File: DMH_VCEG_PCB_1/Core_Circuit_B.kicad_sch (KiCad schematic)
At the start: 111 parts, among them J24 Conn_01x06_PinHeader, J25 Conn_01x10_PinHeader, J26 Conn_01x10_PinHeader, J27 Conn_01x10_PinHeader, Q17 BC558, Q18 BC558, Q19 BC548, Q20 BC548, Q21 BS170, Q22 BS170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

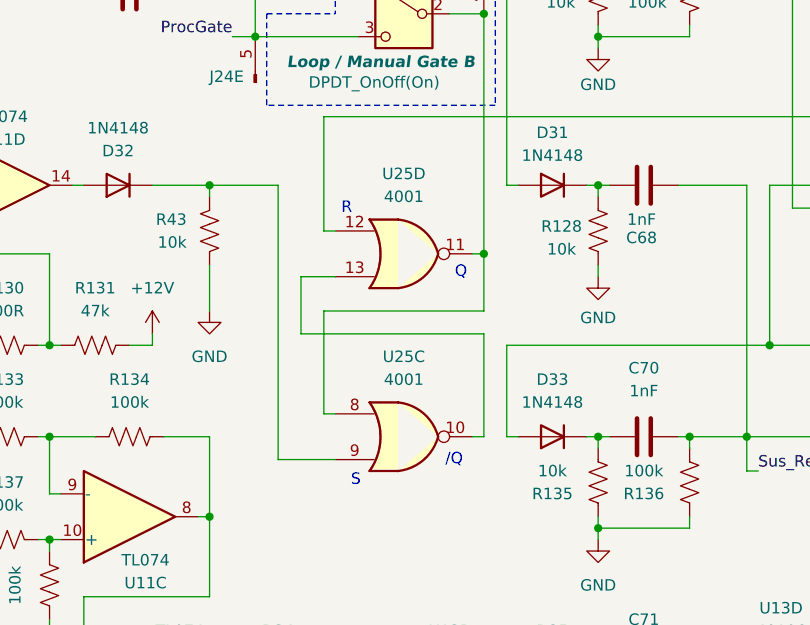
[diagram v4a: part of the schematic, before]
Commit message: PCB 1 placement in progress
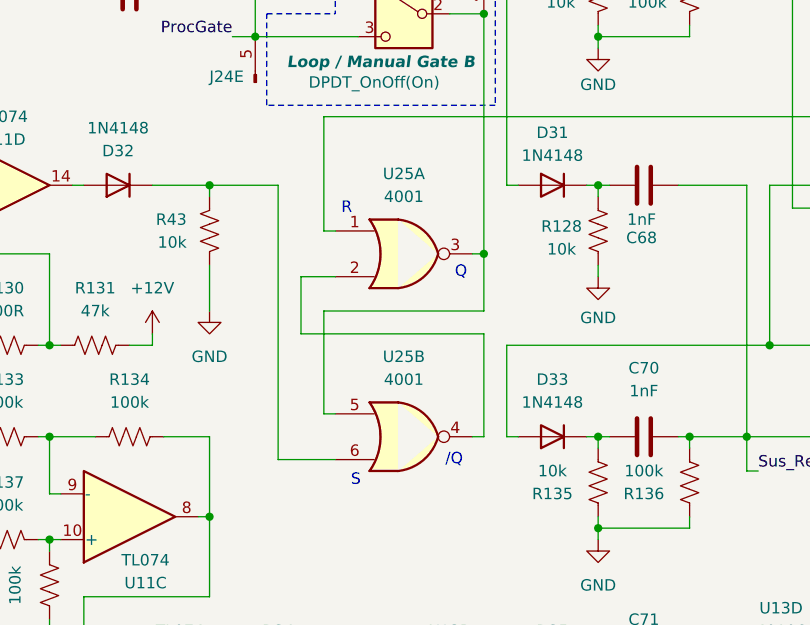
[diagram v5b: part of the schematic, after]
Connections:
- net at D32.1 (K), R43.2: now also U25.6; no longer U25.9
- net at C56.1, R129.1: now also U25.1; no longer U25.12
- net at J24.4 (Pin_4), SW5.2 (B): now also U25.3, U25.5; no longer U25.11, U25.8
- new net: U25.2, U25.4
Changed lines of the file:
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@@
 		(lib_id "4xxx:4001")
 		(at 76.2 151.13 0)
-		(unit 3)
+		(unit 2)
 		(exclude_from_sim no)
 		(in_bom yes)
@@
 				(path "/58f4306d-5387-4983-bb08-41a2313fd315/8d22a13f-1d3b-4a1f-8b3f-baf42965c019"
 					(reference "U25")
-					(unit 3)
+					(unit 2)
 				)
 			)
@@
 		(lib_id "4xxx:4001")
 		(at 76.2 130.81 0)
-		(unit 4)
+		(unit 1)
 		(exclude_from_sim no)
 		(in_bom yes)
@@
 				(path "/58f4306d-5387-4983-bb08-41a2313fd315/8d22a13f-1d3b-4a1f-8b3f-baf42965c019"
 					(reference "U25")
-					(unit 4)
-				)
-			)
+					(unit 1)
+				)
+			)

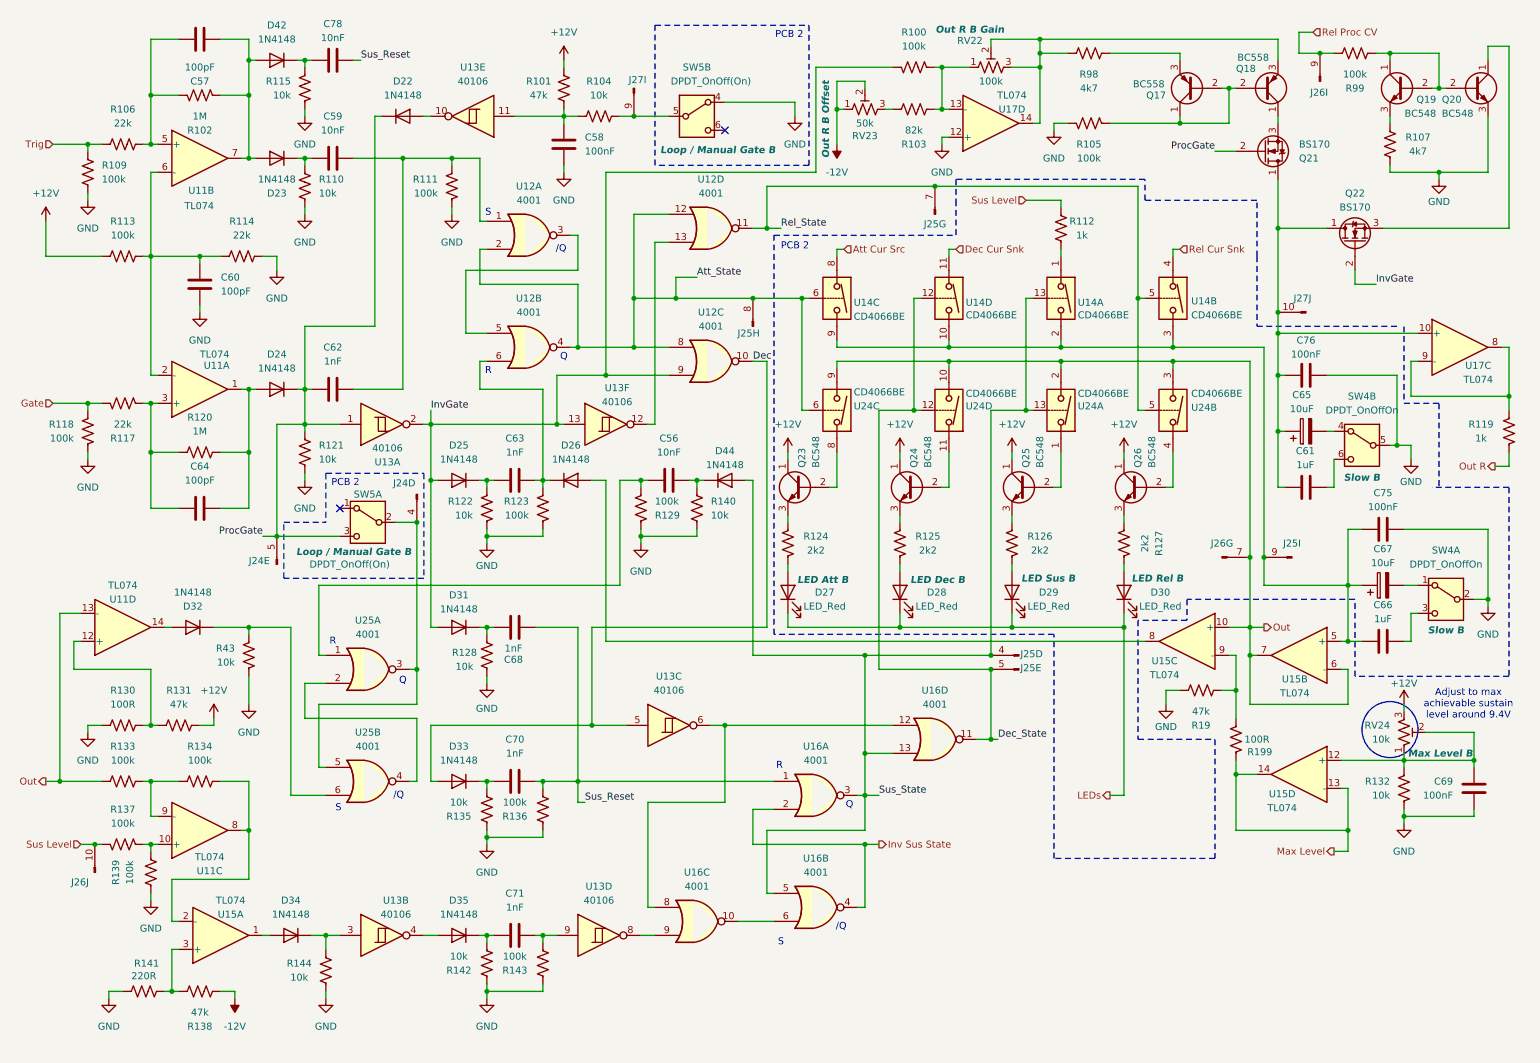
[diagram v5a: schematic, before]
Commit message: PCB 1 circuit A placement done
ciurcuit B placement in progress
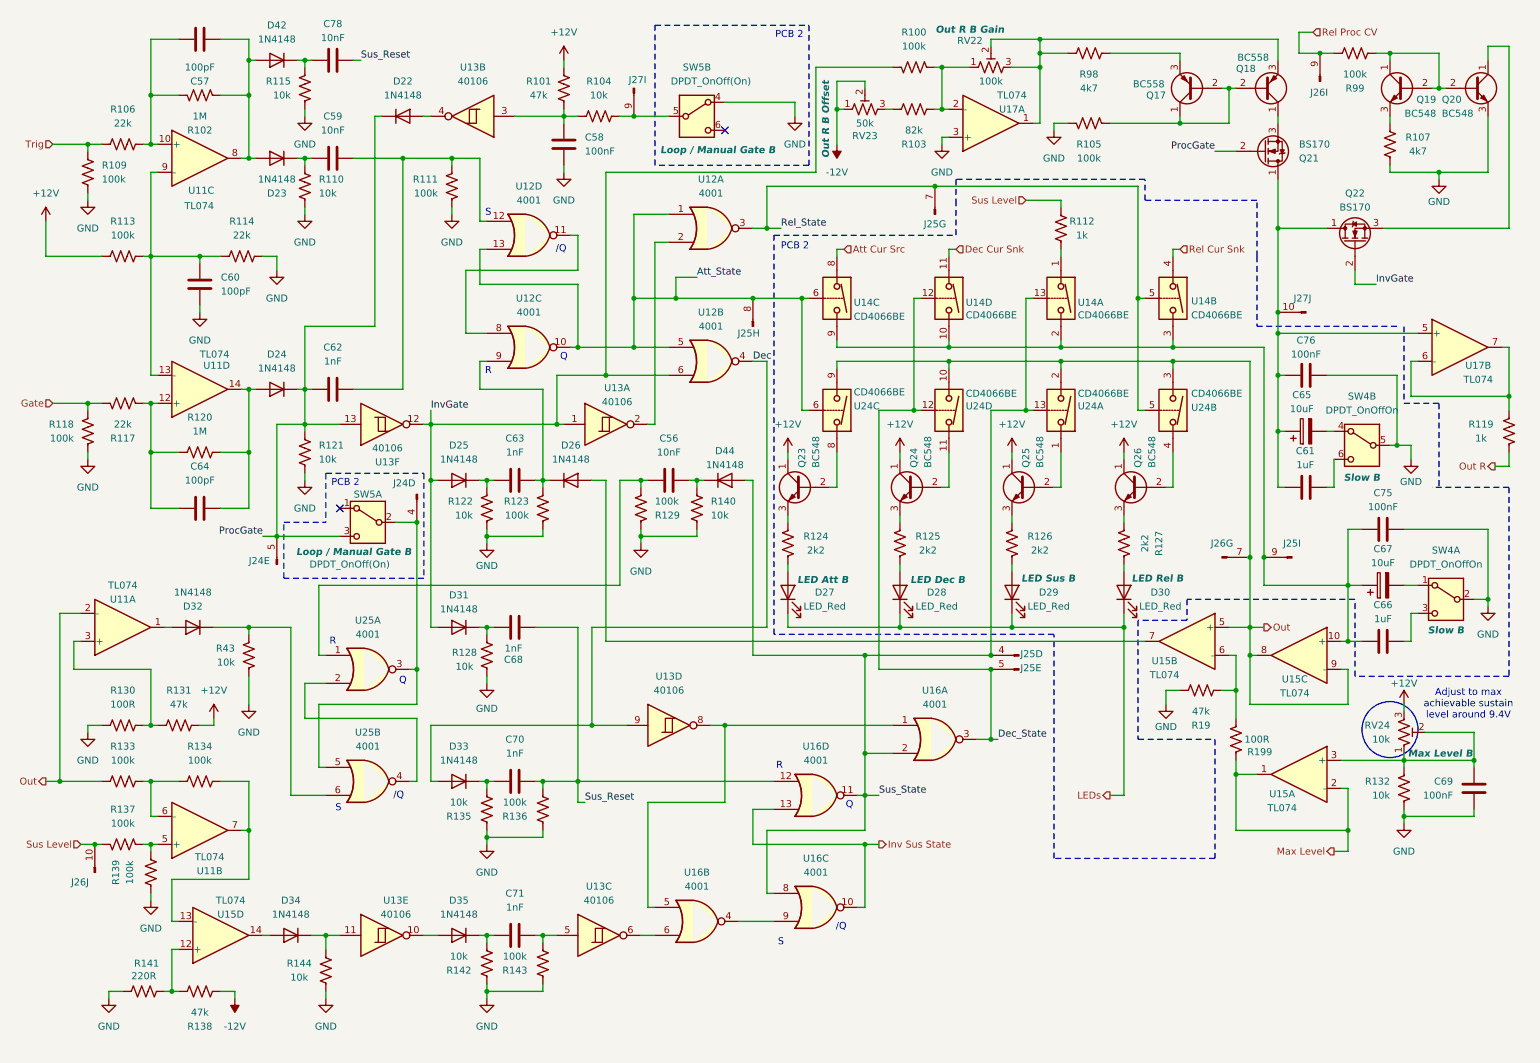
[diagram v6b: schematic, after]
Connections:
- net Att_State: now also U12.1, U12.10, U12.13, U12.5; no longer U12.12, U12.2, U12.4, U12.8
- net Dec: now also U12.4, U13.9; no longer U12.10, U13.5
- net Dec_State: now also U16.3; no longer U16.11
- net GND: now also U17.3 (+); no longer U17.12 (+)
- net Inv Sus State: now also U16.10, U16.13; no longer U16.2, U16.4
- net InvGate: now also U12.6, U13.1, U13.12; no longer U12.9, U13.13, U13.2
- net Max Level: now also U15.1, U15.2 (-); no longer U15.13 (-), U15.14
- net Out: now also U11.2 (-), U15.5 (+), U15.8, U15.9 (-); no longer U11.13 (-), U15.10 (+), U15.6 (-), U15.7
- net ProcGate: now also U13.13; no longer U13.1
- net Rel_State: now also U12.3; no longer U12.11
- net Sus_Reset: now also U16.12; no longer U16.1
- net Sus_State: now also U16.11, U16.2, U16.8; no longer U16.13, U16.3, U16.5
- net at C61.2, C65.1, C76.2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: now also U17.5 (+); no longer U17.10 (+)
- net at D32.2 (A): now also U11.1; no longer U11.14
- net at C60.2, R113.1, R114.2: now also U11.13 (-), U11.9 (-); no longer U11.2 (-), U11.6 (-)
- net at C59.2, C62.2, R111.2: now also U12.12; no longer U12.1
- net at C57.2, D23.2 (A), D42.2 (A)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: now also U11.8; no longer U11.7
- net at R137.2, R139.1: now also U11.5 (+); no longer U11.10 (+)
- net at R133.1, R134.2: now also U11.6 (-); no longer U11.9 (-)
- net at D22.2 (A): now also U13.4; no longer U13.10
- net at R19.2, R199.1: now also U15.6 (-); no longer U15.9 (-)
- net at C63.2, D26.1 (K), R123.2: now also U12.9; no longer U12.6
- net at C64.2, D24.2 (A), R120.1: now also U11.14; no longer U11.1
- net at C64.1, R117.1, R120.2: now also U11.12 (+); no longer U11.3 (+)
- net at D26.2 (A): now also U15.7; no longer U15.8
- net at C58.1, R101.2, R104.2: now also U13.3; no longer U13.11
- net at C69.2, R132.2, RV24.1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: now also U15.3 (+); no longer U15.12 (+)
- net at C66.1, C67.1, C75.2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: now also U15.10 (+); no longer U15.5 (+)
- net at C57.1, R102.2, R106.1: now also U11.10 (+); no longer U11.5 (+)
- net at R100.2, R103.2, RV22.1: now also U17.2 (-); no longer U17.13 (-)
- net at Q18.3 (E), R98.1, RV22.2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: now also U17.1; no longer U17.14
- net at D34.2 (A): now also U15.14; no longer U15.1
- net at R138.1, R141.1: now also U15.12 (+); no longer U15.3 (+)
- net at R130.1, R131.2: now also U11.3 (+); no longer U11.12 (+)
- net at D34.1 (K), R144.1: now also U13.11; no longer U13.3
- net at D35.2 (A): now also U13.10; no longer U13.4
- net at C71.2, R143.1: now also U13.5; no longer U13.9
- new net: R134.1, U11.7, U15.13 (-)
- new net: U12.11, U12.8
- new net: U12.2, U13.2
- new net: U13.8, U16.1, U16.5
- new net: U16.4, U16.9
- new net: U13.6, U16.6
- new net: R119.2, U17.6 (-), U17.7
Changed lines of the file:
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@@
 		(at 45.72 160.02 0)
 		(mirror x)
-		(unit 3)
+		(unit 2)
 		(exclude_from_sim no)
 		(in_bom yes)
@@
 				(path "/58f4306d-5387-4983-bb08-41a2313fd315/8d22a13f-1d3b-4a1f-8b3f-baf42965c019"
 					(reference "U11")
-					(unit 3)
+					(unit 2)
 				)
 			)
@@
 		(lib_id "4xxx:4001")
 		(at 105.41 72.39 0)
-		(unit 2)
+		(unit 3)
 		(exclude_from_sim no)
 		(in_bom yes)
@@
 				(path "/58f4306d-5387-4983-bb08-41a2313fd315/8d22a13f-1d3b-4a1f-8b3f-baf42965c019"
 					(reference "U12")
-					(unit 2)
+					(unit 3)
 				)
 			)
@@
 		(lib_id "4xxx:4001")
 		(at 138.43 74.93 0)
-		(unit 3)
+		(unit 2)
 		(exclude_from_sim no)
 		(in_bom yes)
@@
 				(path "/58f4306d-5387-4983-bb08-41a2313fd315/8d22a13f-1d3b-4a1f-8b3f-baf42965c019"
 					(reference "U12")
-					(unit 3)
+					(unit 2)
 				)
 			)
@@
 		(at 224.79 125.73 0)
 		(mirror y)
-		(unit 3)
+		(unit 2)
 		(exclude_from_sim no)
 		(in_bom yes)
@@
 				(path "/58f4306d-5387-4983-bb08-41a2313fd315/8d22a13f-1d3b-4a1f-8b3f-baf42965c019"
 					(reference "U15")
-					(unit 3)
+					(unit 2)
 				)
 			)
@@
 		(lib_id "4xxx:40106")
 		(at 119.38 86.36 0)
-		(unit 6)
+		(unit 1)
 		(exclude_from_sim no)
 		(in_bom yes)
@@
 				(path "/58f4306d-5387-4983-bb08-41a2313fd315/8d22a13f-1d3b-4a1f-8b3f-baf42965c019"
 					(reference "U13")
-					(unit 6)
+					(unit 1)
 				)
 			)
@@
 		(lib_id "4xxx:40106")
 		(at 95.25 30.48 180)
-		(unit 5)
+		(unit 2)
 		(exclude_from_sim no)
 		(in_bom yes)
@@
 				(path "/58f4306d-5387-4983-bb08-41a2313fd315/8d22a13f-1d3b-4a1f-8b3f-baf42965c019"
 					(reference "U13")
-					(unit 5)
+					(unit 2)
 				)
 			)
@@
 		(lib_id "4xxx:4001")
 		(at 105.41 52.07 0)
-		(unit 1)
+		(unit 4)
 		(exclude_from_sim no)
 		(in_bom yes)
@@
 				(path "/58f4306d-5387-4983-bb08-41a2313fd315/8d22a13f-1d3b-4a1f-8b3f-baf42965c019"
 					(reference "U12")
-					(unit 1)
+					(unit 4)
 				)
 			)
@@
 		(at 245.11 149.86 0)
 		(mirror y)
-		(unit 4)
+		(unit 1)
 		(exclude_from_sim no)
 		(in_bom yes)
@@
 				(path "/58f4306d-5387-4983-bb08-41a2313fd315/8d22a13f-1d3b-4a1f-8b3f-baf42965c019"
 					(reference "U15")
-					(unit 4)
+					(unit 1)
 				)
 			)
@@
 		(at 245.11 128.27 0)
 		(mirror y)
-		(unit 2)
+		(unit 3)
 		(exclude_from_sim no)
 		(in_bom yes)
@@
 				(path "/58f4306d-5387-4983-bb08-41a2313fd315/8d22a13f-1d3b-4a1f-8b3f-baf42965c019"
 					(reference "U15")
-					(unit 2)
+					(unit 3)
 				)
 			)
@@
 		(at 78.74 86.36 0)
 		(mirror x)
-		(unit 1)
+		(unit 6)
 		(exclude_from_sim no)
 		(in_bom yes)
@@
 				(path "/58f4306d-5387-4983-bb08-41a2313fd315/8d22a13f-1d3b-4a1f-8b3f-baf42965c019"
 					(reference "U13")
-					(unit 1)
+					(unit 6)
 				)
 			)
@@
 		(lib_id "4xxx:40106")
 		(at 130.81 140.97 0)
-		(unit 3)
+		(unit 4)
 		(exclude_from_sim no)
 		(in_bom yes)
@@
 				(path "/58f4306d-5387-4983-bb08-41a2313fd315/8d22a13f-1d3b-4a1f-8b3f-baf42965c019"
 					(reference "U13")
-					(unit 3)
+					(unit 4)
 				)
 			)
@@
 		(at 49.53 179.07 0)
 		(mirror x)
-		(unit 1)
+		(unit 4)
 		(exclude_from_sim no)
 		(in_bom yes)
@@
 				(path "/58f4306d-5387-4983-bb08-41a2313fd315/8d22a13f-1d3b-4a1f-8b3f-baf42965c019"
 					(reference "U15")
-					(unit 1)
+					(unit 4)
 				)
 			)
@@
 		(lib_id "4xxx:4001")
 		(at 157.48 153.67 0)
-		(unit 1)
+		(unit 4)
 		(exclude_from_sim no)
 		(in_bom yes)
@@
 				(path "/58f4306d-5387-4983-bb08-41a2313fd315/8d22a13f-1d3b-4a1f-8b3f-baf42965c019"
 					(reference "U16")
-					(unit 1)
+					(unit 4)
 				)
 			)
@@
 		(lib_id "4xxx:4001")
 		(at 135.89 176.53 0)
-		(unit 3)
+		(unit 2)
 		(exclude_from_sim no)
 		(in_bom yes)
@@
 				(path "/58f4306d-5387-4983-bb08-41a2313fd315/8d22a13f-1d3b-4a1f-8b3f-baf42965c019"
 					(reference "U16")
-					(unit 3)
+					(unit 2)
 				)
 			)
@@
 		(lib_id "Amplifier_Operational:TL074")
 		(at 274.32 72.39 0)
-		(unit 3)
+		(unit 2)
 		(exclude_from_sim no)
 		(in_bom yes)
@@
 				(path "/58f4306d-5387-4983-bb08-41a2313fd315/8d22a13f-1d3b-4a1f-8b3f-baf42965c019"
 					(reference "U17")
-					(unit 3)
+					(unit 2)
 				)
 			)
@@
 		(at 189.23 31.75 0)
 		(mirror x)
-		(unit 4)
+		(unit 1)
 		(exclude_from_sim no)
 		(in_bom yes)
@@
 				(path "/58f4306d-5387-4983-bb08-41a2313fd315/8d22a13f-1d3b-4a1f-8b3f-baf42965c019"
 					(reference "U17")
-					(unit 4)
+					(unit 1)
 				)
 			)
@@
 		(lib_id "4xxx:4001")
 		(at 157.48 173.99 0)
-		(unit 2)
+		(unit 3)
 		(exclude_from_sim no)
 		(in_bom yes)
@@
 				(path "/58f4306d-5387-4983-bb08-41a2313fd315/8d22a13f-1d3b-4a1f-8b3f-baf42965c019"
 					(reference "U16")
-					(unit 2)
+					(unit 3)
 				)
 			)
@@
 		(lib_id "4xxx:40106")
 		(at 78.74 179.07 0)
-		(unit 2)
+		(unit 5)
 		(exclude_from_sim no)
 		(in_bom yes)
@@
 				(path "/58f4306d-5387-4983-bb08-41a2313fd315/8d22a13f-1d3b-4a1f-8b3f-baf42965c019"
 					(reference "U13")
-					(unit 2)
+					(unit 5)
 				)
 			)
@@
 		(lib_id "Amplifier_Operational:TL074")
 		(at 45.72 38.1 0)
-		(unit 2)
+		(unit 3)
 		(exclude_from_sim no)
 		(in_bom yes)
@@
 				(path "/58f4306d-5387-4983-bb08-41a2313fd315/8d22a13f-1d3b-4a1f-8b3f-baf42965c019"
 					(reference "U11")
-					(unit 2)
+					(unit 3)
 				)
 			)
@@
 		(at 31.75 123.19 0)
 		(mirror x)
-		(unit 4)
+		(unit 1)
 		(exclude_from_sim no)
 		(in_bom yes)
@@
 				(path "/58f4306d-5387-4983-bb08-41a2313fd315/8d22a13f-1d3b-4a1f-8b3f-baf42965c019"
 					(reference "U11")
-					(unit 4)
+					(unit 1)
 				)
 			)
@@
 		(at 45.72 80.01 0)
 		(mirror x)
-		(unit 1)
+		(unit 4)
 		(exclude_from_sim no)
 		(in_bom yes)
@@
 				(path "/58f4306d-5387-4983-bb08-41a2313fd315/8d22a13f-1d3b-4a1f-8b3f-baf42965c019"
 					(reference "U11")
-					(unit 1)
+					(unit 4)
 				)
 			)
@@
 		(lib_id "4xxx:4001")
 		(at 138.43 50.8 0)
-		(unit 4)
+		(unit 1)
 		(exclude_from_sim no)
 		(in_bom yes)
@@
 				(path "/58f4306d-5387-4983-bb08-41a2313fd315/8d22a13f-1d3b-4a1f-8b3f-baf42965c019"
 					(reference "U12")
-					(unit 4)
+					(unit 1)
 				)
 			)
@@
 		(lib_id "4xxx:40106")
 		(at 118.11 179.07 0)
-		(unit 4)
+		(unit 3)
 		(exclude_from_sim no)
 		(in_bom yes)
@@
 			)
 		)
+		(property "Function" ""
+			(at 118.11 179.07 0)
+			(effects
+				(font
+					(size 1.27 1.27)
+				)
+			)
+		)
 		(pin "3"
 		)
@@
 				(path "/58f4306d-5387-4983-bb08-41a2313fd315/8d22a13f-1d3b-4a1f-8b3f-baf42965c019"
 					(reference "U13")
-					(unit 4)
+					(unit 3)
 				)
 			)
@@
 		(lib_id "4xxx:4001")
 		(at 179.07 143.51 0)
-		(unit 4)
+		(unit 1)
 		(exclude_from_sim no)
 		(in_bom yes)
@@
 				(path "/58f4306d-5387-4983-bb08-41a2313fd315/8d22a13f-1d3b-4a1f-8b3f-baf42965c019"
 					(reference "U16")
-					(unit 4)
+					(unit 1)
 				)
 			)
